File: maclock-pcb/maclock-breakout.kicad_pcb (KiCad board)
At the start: 2 copper layers, 70.5 x 26.5 mm, 25 parts, among them J1 53398-0271, J2 53398-0471, J3 53398-0271, J4 Pi GPIO, SW1 TSB001A3518A, SW2 TSB001A3518A, U1 PAM8302AASCR, U2 SN74LVC1G17DBVR, U3 TPS7A2030PDBVR

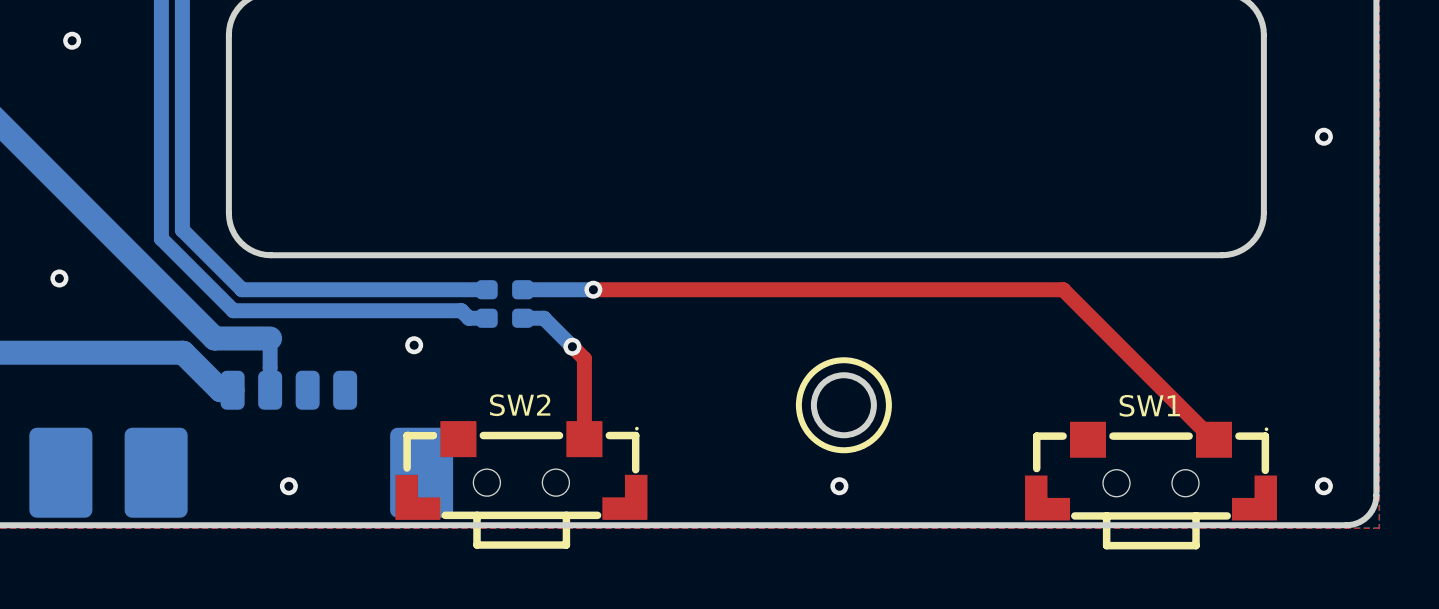
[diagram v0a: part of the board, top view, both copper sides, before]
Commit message: Breakout: source location and licence on the front silkscreen
CERN-OHL-S v2 section 4 asks for the source location on the board's
silkscreen where practicable. "github.com/wr/macintosh-mini   CERN-OHL-S-2.0"
now runs in one line of 0.8 mm text (0.15 stroke) on F.SilkS, centred under
the window at (167, 97.48). The back has no 20 mm free run that isn't pressed
against the switch pegs.

The project sets the silk DRC checks to ignore, so clearance was measured:
the glyphs are 0.28 mm or more from the three tented vias around them
(/SW1, /SW2, GND), and 0.69 mm or more from other silk, pads, holes and the
board edge.

DRC as before (one text-thickness warning), 0 unconnected, schematic parity
clean, with and without --refill-zones; ERC 0.
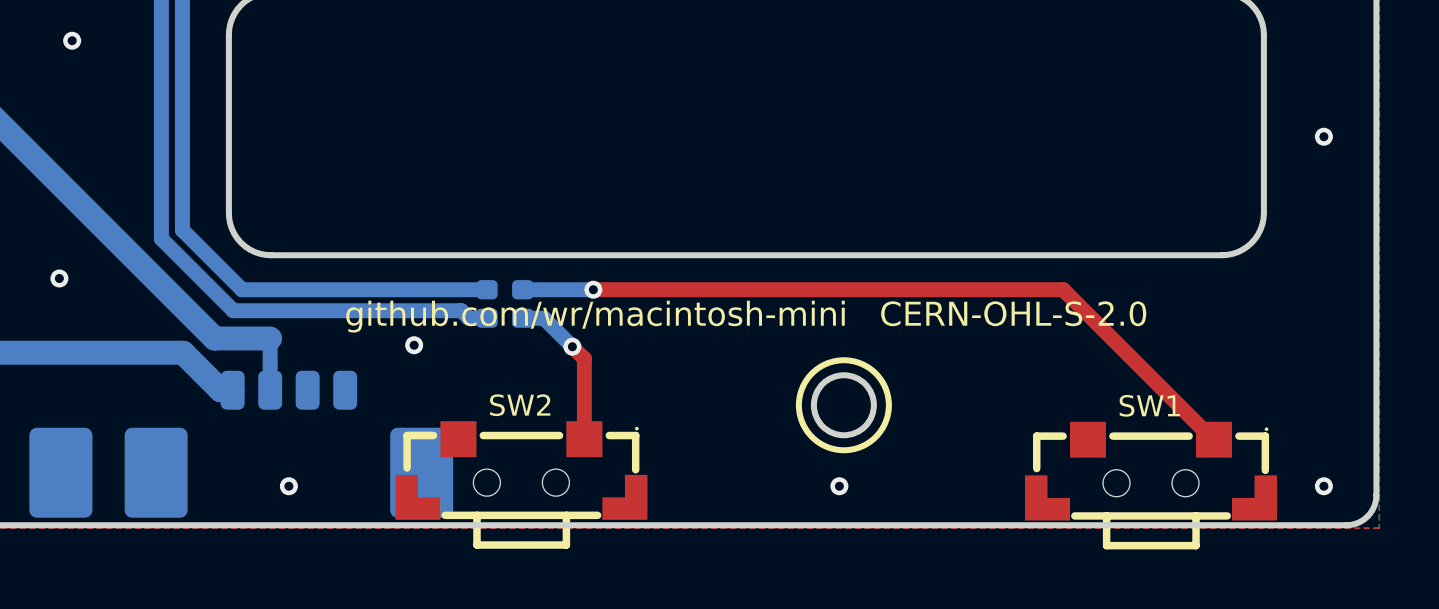
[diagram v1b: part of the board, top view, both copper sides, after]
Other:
- board text added: "github.com/wr/macintosh-mini CERN-OHL-S-2.0"
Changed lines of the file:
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@@
 		(layer "Edge.Cuts")
+	)
+	(gr_text "github.com/wr/macintosh-mini   CERN-OHL-S-2.0"
+		(at 167 97.48 0)
+		(layer "F.SilkS")
+		(effects
+			(font
+				(size 0.8 0.8)
+				(thickness 0.15)
+			)
+		)
 	)
 	(gr_text "eep!"

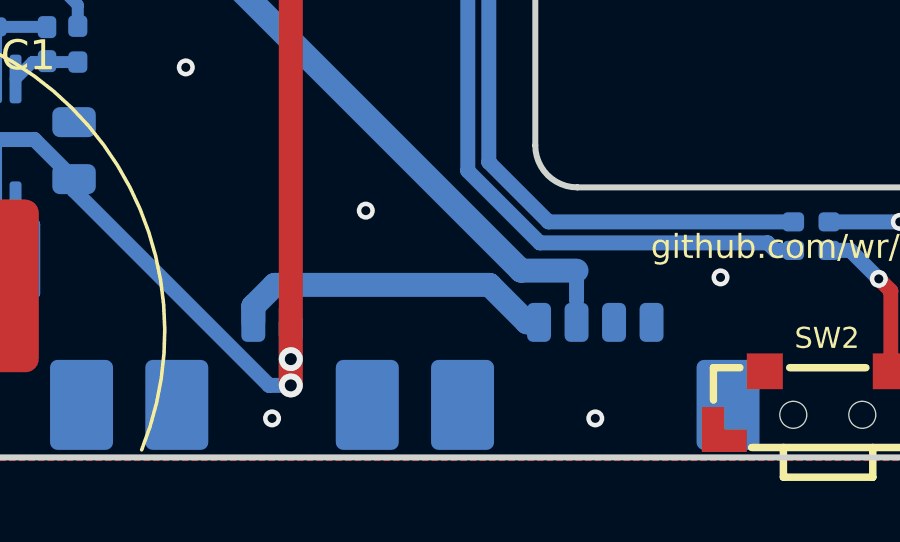
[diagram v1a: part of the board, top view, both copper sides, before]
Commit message: Breakout: Open Source Hardware logo on the front
KiCad's own Symbol:OSHW-Logo_5.7x6mm_SilkScreen (the gear and "open source
hardware", not the OSHWA certification mark, which needs a UID) sits on
F.SilkS at (146.9, 99.75), at the left end of the source and licence line
under the window. It is LOGO1, board-only and out of the BOM and
placement files, so schematic parity and the production BOM and
positions are unchanged.

The project sets the silk DRC checks to ignore, so clearance was measured:
the logo's ink is 0.96 mm from the source line and at least 1.35 mm from
the nearest vias, and its outline is 1.13 mm or more from the board edge.

DRC as before (one text-thickness warning), 0 unconnected, schematic parity
clean, with and without --refill-zones.
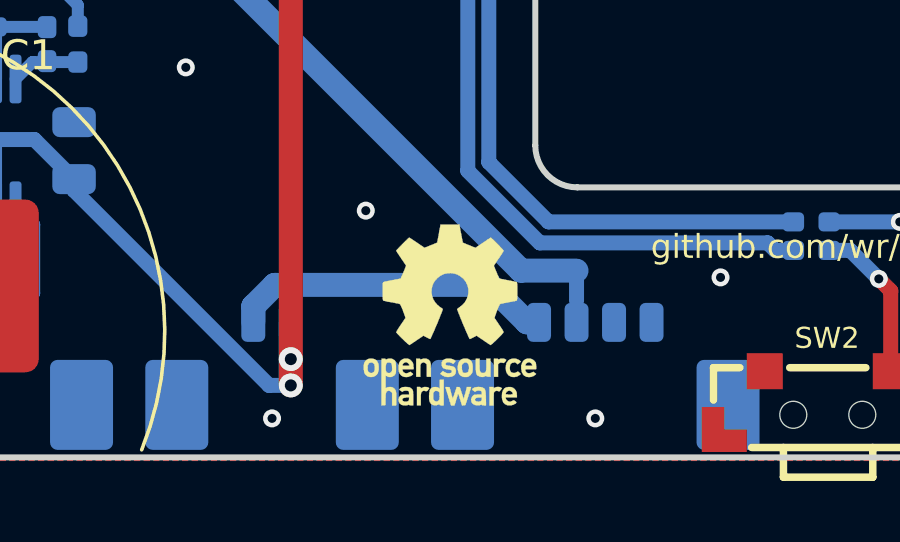
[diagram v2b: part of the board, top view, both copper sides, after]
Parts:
- added LOGO1: OSHW-Logo_5.7x6mm_SilkScreen, Symbol:OSHW-Logo_5.7x6mm_SilkScreen, F.Cu at (146.9, 99.8)

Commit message: Breakout: OSHW logo on the back, beside the amp
LOGO1 moves from the front to B.SilkS, flipped so it reads from the back,
at (144, 92.1). That is the free patch between the amplifier (U1 and its
parts) and the window. Still board-only and out of the BOM and placement
files. The front source and licence line stays where it is.

The project sets the silk DRC checks to ignore, so clearance was measured:
the logo's ink is 0.47 mm and 0.86 mm from the two nearest GND vias, and
its outline is 1.6 mm or more from the J1 label and other silk, and 2.7 mm
or more from pads and the board edge. It sits over the masked B.Cu traces
that cross that patch.

DRC as before (one text-thickness warning), 0 unconnected, schematic parity
clean, with and without --refill-zones.
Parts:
- LOGO1: moved to B.Cu
- moved LOGO1 8.18 mm to (144.0, 92.1), turned to 180 degrees

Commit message: Breakout: centre the OSHW logo between the GPIO traces and the amp
LOGO1 moves from (144, 92.1) to (141.2, 91.45), the middle of its open
patch on the back. The patch runs from C5's pad (x 135.10) to the BTN2
trace (x 147.25), and from the bottom of the header pin labels (y 86.15)
to the top of the "Switch" label (y 96.73). Seen from the back, that is
2.8 mm right and 0.65 mm up.

Clearance, measured on the logo's ink: 0.71 mm to the nearest GND via (up
from 0.47), 2.26 mm or more to other silk, and 2.78 mm or more to pads.

DRC as before (one text-thickness warning), 0 unconnected, schematic parity
clean, with and without --refill-zones. Only the B.Silkscreen gerber
changes.
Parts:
- moved LOGO1 2.87 mm to (141.2, 91.5)
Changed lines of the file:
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@@
 	(footprint "Symbol:OSHW-Logo_5.7x6mm_SilkScreen"
 		(layer "B.Cu")
-		(at 144 92.1 180)
+		(at 141.2 91.45 180)
 		(descr "Open Source Hardware Logo")
 		(tags "Logo OSHW")

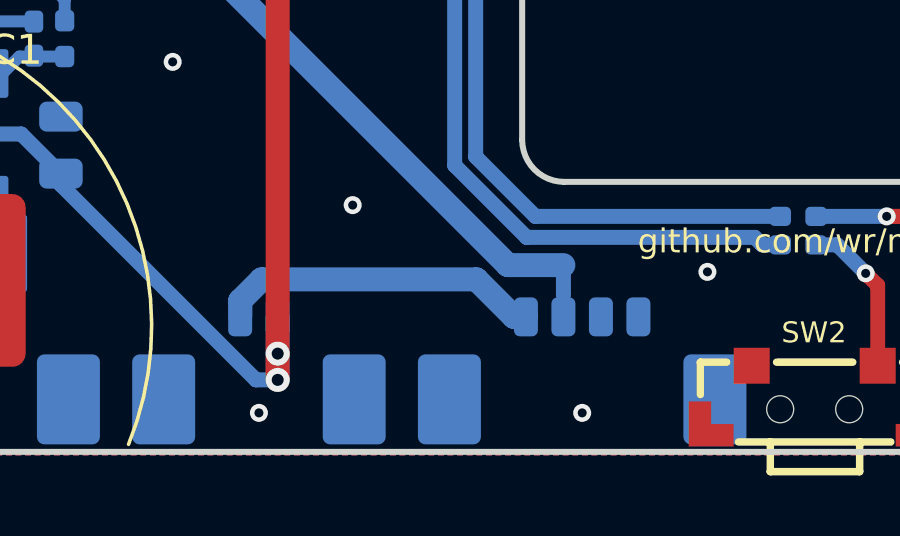
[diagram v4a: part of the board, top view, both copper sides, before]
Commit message: Breakout: J2 power is pin 1 (+) and pin 2 (GND), not pins 4 and 3
The Maclock's 4-wire plug puts the battery supply on PicoBlade pin 1 and
ground on pin 2. The board had them on pins 4 and 3, inherited from the
JST SH version, so a rev 2026.11 board would not have powered up from the
clock's own plug.

Board: J2 pad 1 = /5V_IN, pad 2 = GND, pads 3-4 unconnected. /5V_IN now
leaves its lane early, drops between J2's west mounting tab and pad 4
(0.6 mm there, 0.3 mm clear of both), runs under the pads at y 101.6 and
comes up into pad 1 from the south, all on B.Cu, no vias. NT1 and the
GND_PI trace end move 1.25 mm east so the net tie still lands on J2's
ground pad, and the silk '+' / '-' move over pads 1 / 2.

Schematic: J2 pin 1 wired to 5V_IN, pin 2 to GND, pins 3-4 no-connect;
power-block note updated. ERC 0, DRC at baseline (the one Macintosh Mini
text_thickness warning), 0 unconnected, parity clean.
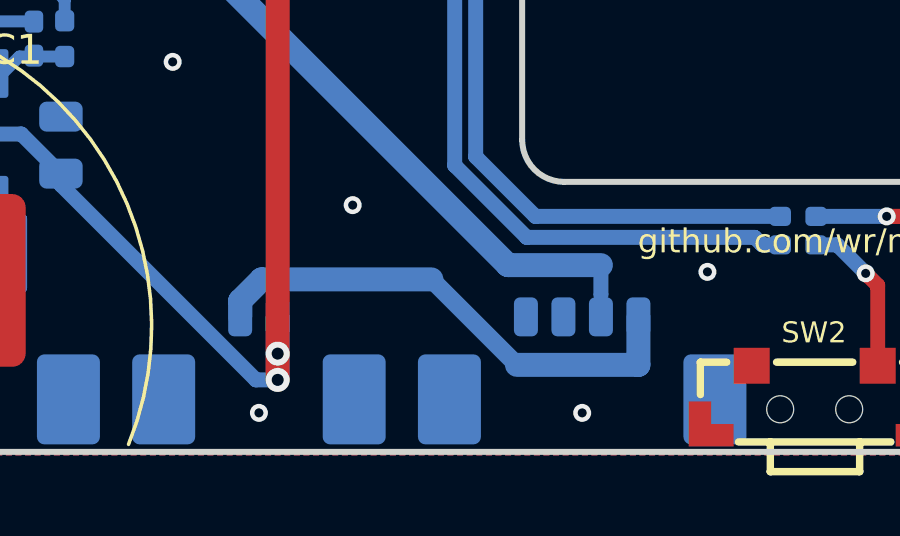
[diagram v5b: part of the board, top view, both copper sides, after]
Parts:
- moved NT1 1.25 mm to (152.4, 98.8)
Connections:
- J2 pad 1: unconnected-(J2-Pin_1-Pad1) -> /5V_IN
- J2 pad 2: unconnected-(J2-Pin_2-Pad2) -> GND
- J2 pad 3: GND -> unconnected-(J2-Pin_3-Pad3)
- J2 pad 4: /5V_IN -> unconnected-(J2-Pin_4-Pad4)
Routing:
- net /5V_IN: track 10.9 -> 16.9 mm
- net /GND_PI: track 26.3 -> 27.5 mm
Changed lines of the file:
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@@
 	(footprint "NetTie:NetTie-2_SMD_Pad0.5mm"
 		(layer "B.Cu")
-		(at 151.125 98.775 -90)
+		(at 152.375 98.775 -90)
 		(descr "Net tie, 2 pin, 0.5mm square SMD pads")
 		(tags "net tie")
@@
 			(layers "B.Cu" "B.Mask" "B.Paste")
 			(roundrect_rratio 0.25)
-			(net "unconnected-(J2-Pin_1-Pad1)")
+			(net "/5V_IN")
 		)
 		(pad "2" smd roundrect
@@
 			(layers "B.Cu" "B.Mask" "B.Paste")
 			(roundrect_rratio 0.25)
-			(net "unconnected-(J2-Pin_2-Pad2)")
+			(net "GND")
 		)
 		(pad "3" smd roundrect
@@
 			(layers "B.Cu" "B.Mask" "B.Paste")
 			(roundrect_rratio 0.25)
-			(net "GND")
+			(net "unconnected-(J2-Pin_3-Pad3)")
 		)
 		(pad "4" smd roundrect
@@
 			(layers "B.Cu" "B.Mask" "B.Paste")
 			(roundrect_rratio 0.25)
-			(net "/5V_IN")
+			(net "unconnected-(J2-Pin_4-Pad4)")
 		)
 		(pad "MP" smd roundrect
@@
 		)
 	)
-	(gr_text "+"
-		(at 149.9 98.675 0)
+	(gr_text "-"
+		(at 152.4 98.675 0)
 		(layer "B.SilkS")
 		(effects
@@
 		)
 	)
-	(gr_text "-"
-		(at 151.15 98.675 0)
+	(gr_text "+"
+		(at 153.65 98.675 0)
 		(layer "B.SilkS")
 		(effects
@@
 	(segment
 		(start 149.275 98.275)
-		(end 151.125 98.275)
+		(end 152.375 98.275)
 		(width 0.8)
 		(layer "B.Cu")
@@
 	)
 	(segment
-		(start 140.35 99.463088)
-		(end 141.063088 98.75)
-		(width 0.8)
+		(start 146.725 98.75)
+		(end 149.575 101.6)
+		(width 0.6)
 		(layer "B.Cu")
 		(net "/5V_IN")
 	)
 	(segment
-		(start 148.225 98.75)
-		(end 149.475 100)
+		(start 140.35 99.463088)
+		(end 141.063088 98.75)
 		(width 0.8)
 		(layer "B.Cu")
@@
 	(segment
 		(start 141.063088 98.75)
-		(end 148.225 98.75)
+		(end 146.725 98.75)
 		(width 0.8)
 		(layer "B.Cu")
@@
 	)
 	(segment
-		(start 149.475 100)
-		(end 149.875 100)
+		(start 153.625 101.6)
+		(end 153.625 100)
 		(width 0.8)
 		(layer "B.Cu")
@@
 		(width 0.8)
 		(layer "B.Cu")
+		(net "/5V_IN")
+	)
+	(segment
+		(start 149.575 101.6)
+		(end 153.625 101.6)
+		(width 0.8)
+		(layer "B.Cu")

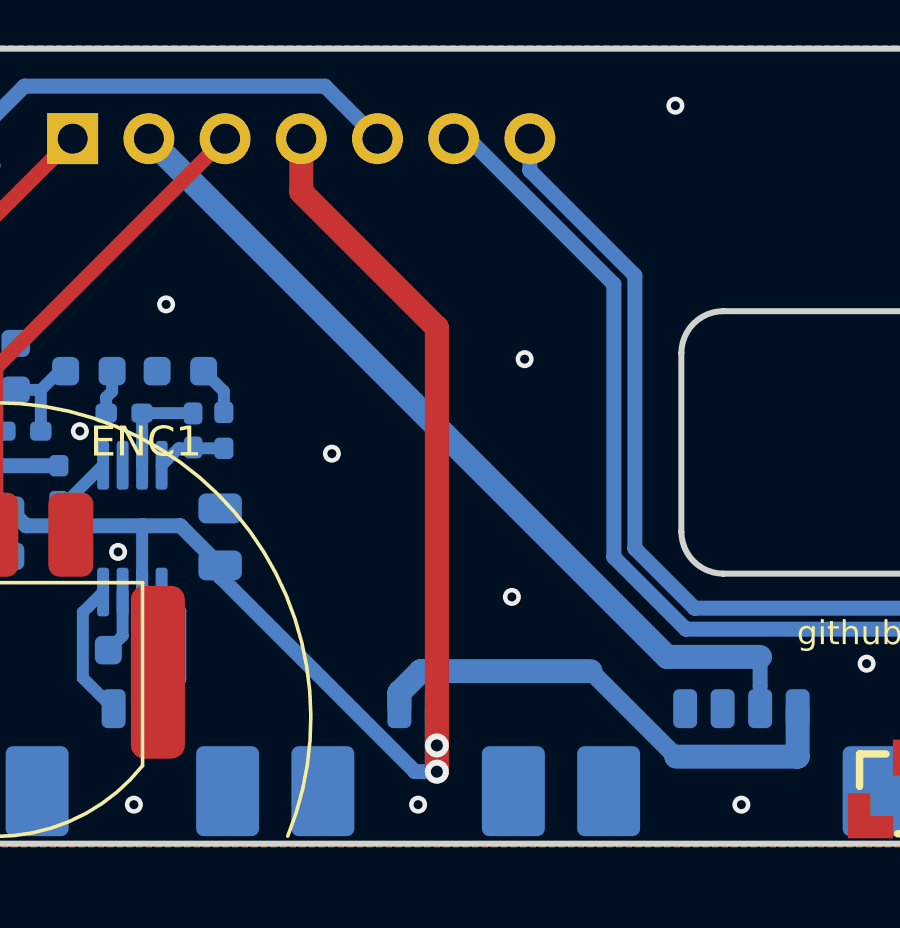
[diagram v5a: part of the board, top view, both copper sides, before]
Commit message: Breakout: straighter power routing at J1/J2; J1's pins swap to match
Layout (hand-routed in KiCad): /5V_IN now runs straight along the
connector row at y 100 from J2 pad 1 into J1 pad 1, then dips under J2
at 0.8 mm (0.28 mm from J2 pad 4, 0.31 mm from its mounting tab). +5V
leaves J1 pad 2 up to one 0.8/0.4 via at (140.35, 98.725) and the F.Cu
trunk goes straight north from there, so the trunk no longer runs down
to the board edge; the amp's 0.5 mm feed taps J1 pad 2. J1 is the power
switch, so which pad is which does not matter electrically.

Schematic follows the swap: J1 pin 1 = 5V_IN, pin 2 = +5V. 5V_IN is now
one wire from J2 pin 1 to J1 pin 1; the +5V arrow and its PWR_FLAG sit
on J1 pin 2's wire. ERC 0, DRC at baseline (the Macintosh Mini
text_thickness warning), 0 unconnected, parity clean.
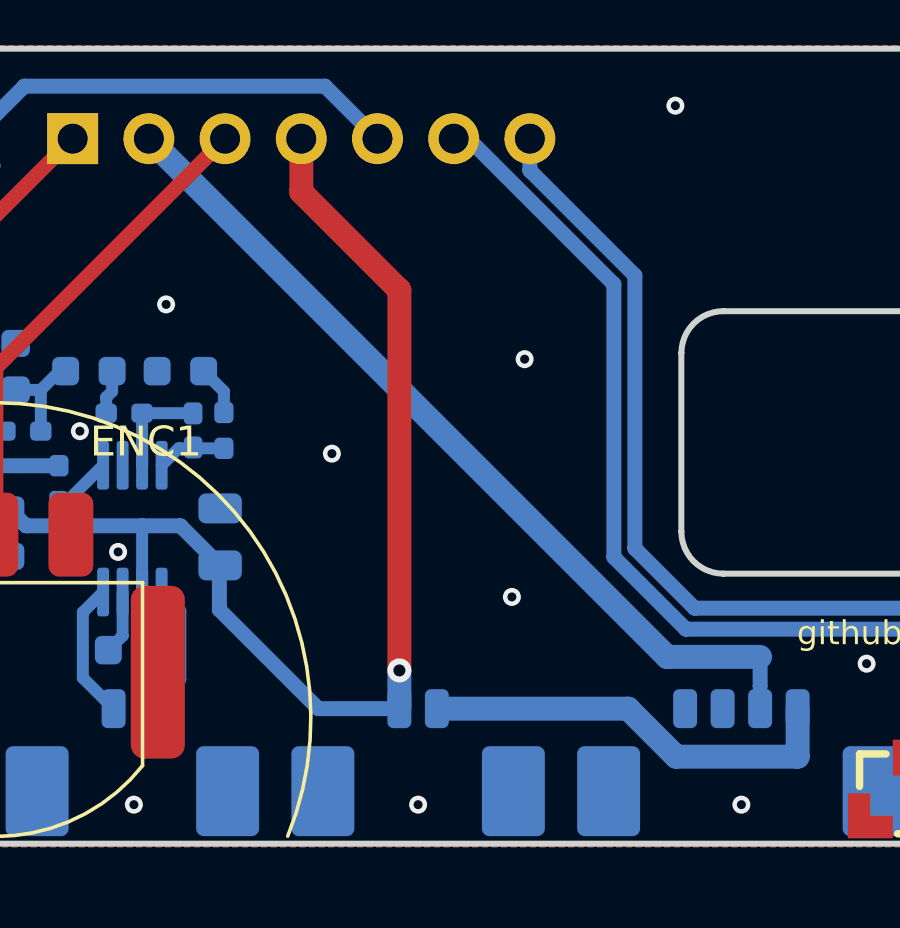
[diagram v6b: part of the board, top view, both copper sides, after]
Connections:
- J1 pad 1: +5V -> /5V_IN
- J1 pad 2: /5V_IN -> +5V
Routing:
- net +5V: track 52.9 -> 46.7 mm, vias 2 -> 1
- net /5V_IN: track 16.9 -> 14.3 mm
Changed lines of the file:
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@@
 		)
 		(property "Label" "Speaker"
-			(at 6.449999 0.95 0)
+			(at 5.499999 1.225 0)
 			(layer "B.SilkS")
 			(effects
@@
 			(layers "B.Cu" "B.Mask" "B.Paste")
 			(roundrect_rratio 0.25)
-			(net "+5V")
+			(net "/5V_IN")
 		)
 		(pad "2" smd roundrect
@@
 			(layers "B.Cu" "B.Mask" "B.Paste")
 			(roundrect_rratio 0.25)
-			(net "/5V_IN")
+			(net "+5V")
 		)
 		(pad "MP" smd roundrect
@@
 	)
 	(segment
-		(start 141.6 102.1)
-		(end 141.6 87.297793)
+		(start 140.35 98.725)
+		(end 140.35 86.047793)
 		(width 0.8)
 		(layer "F.Cu")
@@
 	)
 	(segment
-		(start 141.6 87.297793)
+		(start 140.35 86.047793)
 		(end 137.08 82.777793)
 		(width 0.8)
@@
 	)
 	(via
-		(at 141.6 102.1)
-		(size 0.8)
-		(drill 0.4)
-		(layers "F.Cu" "B.Cu")
-		(net "+5V")
-	)
-	(via
-		(at 141.6 101.225)
+		(at 140.35 98.725)
 		(size 0.8)
 		(drill 0.4)
 		(layers "F.Cu" "B.Cu")
+		(free yes)
 		(net "+5V")
 	)
@@
 	)
 	(segment
-		(start 141.6 102.1)
-		(end 141.6 101.225)
-		(width 0.8)
+		(start 137.65 100)
+		(end 140.35 100)
+		(width 0.5)
 		(layer "B.Cu")
 		(net "+5V")
 	)
 	(segment
-		(start 134.375 95.225)
-		(end 134.375 95.59978)
+		(start 127.375 93.375)
+		(end 127.905 93.905)
 		(width 0.5)
 		(layer "B.Cu")
@@
 	)
 	(segment
-		(start 127.375 93.375)
-		(end 127.905 93.905)
+		(start 134.35 96.7)
+		(end 137.65 100)
 		(width 0.5)
 		(layer "B.Cu")
@@
 	)
 	(segment
+		(start 140.35 100)
+		(end 140.35 98.725)
+		(width 0.8)
+		(layer "B.Cu")
+		(net "+5V")
+	)
+	(segment
 		(start 131.774999 96.1125)
 		(end 131.774999 97.6275)
@@
 	)
 	(segment
-		(start 134.375 95.59978)
-		(end 140.87522 102.1)
+		(start 125.4375 93.375)
+		(end 124.872316 93.375)
 		(width 0.5)
 		(layer "B.Cu")
@@
 	)
 	(segment
-		(start 125.4375 93.375)
-		(end 124.872316 93.375)
+		(start 134.35 95.25)
+		(end 134.35 96.7)
 		(width 0.5)
 		(layer "B.Cu")
@@
 	)
 	(segment
-		(start 140.87522 102.1)
-		(end 141.6 102.1)
+		(start 134.375 95.225)
+		(end 134.35 95.25)
 		(width 0.5)
 		(layer "B.Cu")
@@
 	)
 	(segment
-		(start 141.6 101.225)
-		(end 141.6 100)
-		(width 0.8)
-		(layer "B.Cu")
-		(net "+5V")
-	)
-	(segment
 		(start 142.65 81)
 		(end 147.5 85.85)
@@
 	)
 	(segment
-		(start 146.725 98.75)
-		(end 149.575 101.6)
-		(width 0.6)
+		(start 149.575 101.6)
+		(end 153.625 101.6)
+		(width 0.8)
 		(layer "B.Cu")
 		(net "/5V_IN")
 	)
 	(segment
-		(start 140.35 99.463088)
-		(end 141.063088 98.75)
+		(start 147.975 100)
+		(end 149.575 101.6)
 		(width 0.8)
 		(layer "B.Cu")
@@
 	)
 	(segment
-		(start 141.063088 98.75)
-		(end 146.725 98.75)
+		(start 141.6 100)
+		(end 147.975 100)
 		(width 0.8)
 		(layer "B.Cu")
@@
 		(width 0.8)
 		(layer "B.Cu")
-		(net "/5V_IN")
-	)
-	(segment
-		(start 140.35 100)
-		(end 140.35 99.463088)
-		(width 0.8)
-		(layer "B.Cu")
-		(net "/5V_IN")
-	)
-	(segment
-		(start 149.575 101.6)
-		(end 153.625 101.6)
-		(width 0.8)
-		(layer "B.Cu")
